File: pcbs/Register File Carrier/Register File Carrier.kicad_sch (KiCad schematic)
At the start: 2 parts, among them J1001 Conn_02x20_Odd_Even, J1002 Conn_02x20_Odd_Even

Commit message: Roughing a little more out
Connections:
- no-connect marks 22 -> 10
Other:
- sheet Connector Block ports: added A[0..15], B[0..15], CLK, C[0..15], R_{A}[0..3], R_{B}[0..3], R_{C}[0..3], ~{Active}; removed none
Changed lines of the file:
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@@
-	)
-	(no_connect
-		(at 26.67 128.27)
 	)
 	(no_connect
@@
 	)
 	(no_connect
-		(at 44.45 133.35)
-	)
-	(no_connect
 		(at 44.45 138.43)
-	)
-	(no_connect
-		(at 26.67 130.81)
-	)
-	(no_connect
-		(at 44.45 130.81)
-	)
-	(no_connect
-		(at 26.67 123.19)
-	)
-	(no_connect
-		(at 44.45 135.89)
 	)
 	(no_connect
@@
 	)
 	(no_connect
-		(at 26.67 125.73)
-	)
-	(no_connect
 		(at 29.21 76.2)
 	)
@@
 	)
 	(no_connect
-		(at 44.45 123.19)
-	)
-	(no_connect
 		(at 41.91 76.2)
-	)
-	(no_connect
-		(at 44.45 128.27)
 	)
 	(no_connect
@@
 	)
 	(no_connect
-		(at 26.67 133.35)
-	)
-	(no_connect
-		(at 26.67 135.89)
-	)
-	(no_connect
-		(at 44.45 125.73)
-	)
-	(no_connect
 		(at 41.91 143.51)
 	)
@@
 		)
 	)
+	(bus
+		(pts
+			(xy 127 115.57) (xy 137.16 115.57)
+		)
+		(stroke
+			(width 0)
+			(type default)
+		)
+	)
 	(wire
 		(pts
@@
 		)
 	)
+	(bus
+		(pts
+			(xy 127 118.11) (xy 137.16 118.11)
+		)
+		(stroke
+			(width 0)
+			(type default)
+		)
+	)
 	(wire
 		(pts
@@
 		(pts
 			(xy 26.67 138.43) (xy 29.21 138.43)
+		)
+		(stroke
+			(width 0)
+			(type default)
+		)
+	)
+	(bus
+		(pts
+			(xy 127 120.65) (xy 137.16 120.65)
 		)
 		(stroke
@@
 	)
 	(sheet
-		(at 137.16 92.71)
-		(size 107.95 73.66)
+		(at 137.16 114.3)
+		(size 36.83 54.61)
 		(fields_autoplaced yes)
 		(stroke
@@
 		)
 		(property "Sheetname" "Connector Block"
-			(at 137.16 91.9984 0)
+			(at 137.16 113.5884 0)
 			(effects
 				(font
@@
 		)
 		(property "Sheetfile" "connectors.kicad_sch"
-			(at 137.16 166.9546 0)
+			(at 137.16 169.4946 0)
 			(effects
 				(font
@@
 			)
 		)
+		(pin "~{Active}" input
+			(at 137.16 151.13 180)
+			(effects
+				(font
+					(size 1.27 1.27)
+				)
+				(justify left)
+			)
+		)
+		(pin "CLK" input
+			(at 137.16 148.59 180)
+			(effects
+				(font
+					(size 1.27 1.27)
+				)
+				(justify left)
+			)
+		)
+		(pin "C[0..15]" input
+			(at 137.16 146.05 180)
+			(effects
+				(font
+					(size 1.27 1.27)
+				)
+				(justify left)
+			)
+		)
+		(pin "R_{A}[0..3]" input
+			(at 137.16 115.57 180)
+			(effects
+				(font
+					(size 1.27 1.27)
+				)
+				(justify left)
+			)
+		)
+		(pin "R_{C}[0..3]" input
+			(at 137.16 120.65 180)
+			(effects
+				(font
+					(size 1.27 1.27)
+				)
+				(justify left)
+			)
+		)
+		(pin "R_{B}[0..3]" input
+			(at 137.16 118.11 180)
+			(effects
+				(font
+					(size 1.27 1.27)
+				)
+				(justify left)
+			)
+		)
+		(pin "A[0..15]" output
+			(at 137.16 128.27 180)
+			(effects
+				(font
+					(size 1.27 1.27)
+				)
+				(justify left)
+			)
+		)
+		(pin "B[0..15]" output
+			(at 137.16 132.08 180)
+			(effects
+				(font
+					(size 1.27 1.27)
+				)
+				(justify left)
+			)
+		)

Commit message: Working on register selectors
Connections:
- net I10 renamed R_{B}2
- net I11 renamed R_{B}3
- net I12 renamed R_{C}0
- net I13 renamed R_{C}1
- net I14 renamed R_{C}2
- net I15 renamed R_{C}3
- net I4 renamed R_{A}0
- net I5 renamed R_{A}1
- net I6 renamed R_{A}2
- net I7 renamed R_{A}3
- net I8 renamed R_{B}0
- net I9 renamed R_{B}1
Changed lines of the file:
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@@
-		)
-	)
-	(label "I7"
-		(at 44.45 125.73 0)
-		(fields_autoplaced yes)
-		(effects
-			(font
-				(size 1.27 1.27)
-			)
-			(justify left bottom)
 		)
 	)
@@
 		)
 	)
+	(label "R_{B}3"
+		(at 44.45 130.81 0)
+		(fields_autoplaced yes)
+		(effects
+			(font
+				(size 1.27 1.27)
+			)
+			(justify left bottom)
+		)
+	)
 	(label "C7"
 		(at 44.45 105.41 0)
@@
 		)
 	)
+	(label "R_{C}0"
+		(at 26.67 133.35 180)
+		(fields_autoplaced yes)
+		(effects
+			(font
+				(size 1.27 1.27)
+			)
+			(justify right bottom)
+		)
+	)
 	(label "A10"
 		(at 26.67 48.26 180)
@@
 		)
 	)
+	(label "R_{C}2"
+		(at 26.67 135.89 180)
+		(fields_autoplaced yes)
+		(effects
+			(font
+				(size 1.27 1.27)
+			)
+			(justify right bottom)
+		)
+	)
 	(label "Cycle1"
 		(at 44.45 138.43 0)
@@
 		)
 	)
-	(label "I9"
-		(at 44.45 128.27 0)
-		(fields_autoplaced yes)
-		(effects
-			(font
-				(size 1.27 1.27)
-			)
-			(justify left bottom)
-		)
-	)
-	(label "I6"
-		(at 26.67 125.73 180)
-		(fields_autoplaced yes)
-		(effects
-			(font
-				(size 1.27 1.27)
-			)
-			(justify right bottom)
+	(label "R_{B}2"
+		(at 26.67 130.81 180)
+		(fields_autoplaced yes)
+		(effects
+			(font
+				(size 1.27 1.27)
+			)
+			(justify right bottom)
+		)
+	)
+	(label "R_{C}1"
+		(at 44.45 133.35 0)
+		(fields_autoplaced yes)
+		(effects
+			(font
+				(size 1.27 1.27)
+			)
+			(justify left bottom)
 		)
 	)
@@
 		)
 	)
+	(label "R_{B}1"
+		(at 44.45 128.27 0)
+		(fields_autoplaced yes)
+		(effects
+			(font
+				(size 1.27 1.27)
+			)
+			(justify left bottom)
+		)
+	)
 	(label "B2"
 		(at 26.67 58.42 180)
@@
 		)
 	)
-	(label "I11"
-		(at 44.45 130.81 0)
-		(fields_autoplaced yes)
-		(effects
-			(font
-				(size 1.27 1.27)
-			)
-			(justify left bottom)
-		)
-	)
-	(label "I4"
+	(label "R_{A}0"
 		(at 26.67 123.19 180)
 		(fields_autoplaced yes)
@@
 		)
 	)
+	(label "R_{A}1"
+		(at 44.45 123.19 0)
+		(fields_autoplaced yes)
+		(effects
+			(font
+				(size 1.27 1.27)
+			)
+			(justify left bottom)
+		)
+	)
 	(label "C2"
 		(at 26.67 100.33 180)
@@
 		)
 	)
+	(label "R_{A}2"
+		(at 26.67 125.73 180)
+		(fields_autoplaced yes)
+		(effects
+			(font
+				(size 1.27 1.27)
+			)
+			(justify right bottom)
+		)
+	)
 	(label "A3"
 		(at 44.45 38.1 0)
@@
 		)
 	)
+	(label "R_{C}3"
+		(at 44.45 135.89 0)
+		(fields_autoplaced yes)
+		(effects
+			(font
+				(size 1.27 1.27)
+			)
+			(justify left bottom)
+		)
+	)
 	(label "I1"
 		(at 44.45 118.11 0)
@@
 		)
 	)
-	(label "I8"
-		(at 26.67 128.27 180)
-		(fields_autoplaced yes)
-		(effects
-			(font
-				(size 1.27 1.27)
-			)
-			(justify right bottom)
-		)
-	)
 	(label "A2"
 		(at 26.67 38.1 180)
@@
 		)
 	)
+	(label "R_{A}3"
+		(at 44.45 125.73 0)
+		(fields_autoplaced yes)
+		(effects
+			(font
+				(size 1.27 1.27)
+			)
+			(justify left bottom)
+		)
+	)
 	(label "A8"
 		(at 26.67 45.72 180)
@@
 		)
 	)
-	(label "I15"
-		(at 44.45 135.89 0)
-		(fields_autoplaced yes)
-		(effects
-			(font
-				(size 1.27 1.27)
-			)
-			(justify left bottom)
-		)
-	)
 	(label "C11"
 		(at 44.45 110.49 0)
@@
 		)
 	)
-	(label "I12"
-		(at 26.67 133.35 180)
-		(fields_autoplaced yes)
-		(effects
-			(font
-				(size 1.27 1.27)
-			)
-			(justify right bottom)
-		)
-	)
 	(label "C15"
 		(at 44.45 115.57 0)
@@
 		)
 	)
-	(label "I5"
-		(at 44.45 123.19 0)
-		(fields_autoplaced yes)
-		(effects
-			(font
-				(size 1.27 1.27)
-			)
-			(justify left bottom)
-		)
-	)
 	(label "B9"
 		(at 44.45 66.04 0)
@@
 		)
 	)
-	(label "I14"
-		(at 26.67 135.89 180)
-		(fields_autoplaced yes)
-		(effects
-			(font
-				(size 1.27 1.27)
-			)
-			(justify right bottom)
-		)
-	)
 	(label "B8"
 		(at 26.67 66.04 180)
@@
 		)
 	)
+	(label "R_{B}0"
+		(at 26.67 128.27 180)
+		(fields_autoplaced yes)
+		(effects
+			(font
+				(size 1.27 1.27)
+			)
+			(justify right bottom)
+		)
+	)
 	(label "C4"
 		(at 26.67 102.87 180)
@@
 		)
 	)
-	(label "I10"
-		(at 26.67 130.81 180)
-		(fields_autoplaced yes)
-		(effects
-			(font
-				(size 1.27 1.27)
-			)
-			(justify right bottom)
-		)
-	)
 	(label "C13"
 		(at 44.45 113.03 0)
-		(fields_autoplaced yes)
-		(effects
-			(font
-				(size 1.27 1.27)
-			)
-			(justify left bottom)
-		)
-	)
-	(label "I13"
-		(at 44.45 133.35 0)
 		(fields_autoplaced yes)
 		(effects
@@
 	(sheet
 		(at 137.16 114.3)
-		(size 36.83 54.61)
+		(size 22.86 34.29)
 		(fields_autoplaced yes)
 		(stroke
@@
 		)
 		(property "Sheetfile" "connectors.kicad_sch"
-			(at 137.16 169.4946 0)
+			(at 137.16 149.1746 0)
 			(effects
 				(font
@@
 		)
 		(pin "~{Active}" input
-			(at 137.16 151.13 180)
+			(at 137.16 140.97 180)
 			(effects
 				(font
@@
 		)
 		(pin "CLK" input
-			(at 137.16 148.59 180)
+			(at 137.16 138.43 180)
 			(effects
 				(font
@@
 		)
 		(pin "C[0..15]" input
-			(at 137.16 146.05 180)
-			(effects
-				(font
+			(at 137.16 134.62 180)
+			(effects
+				(font

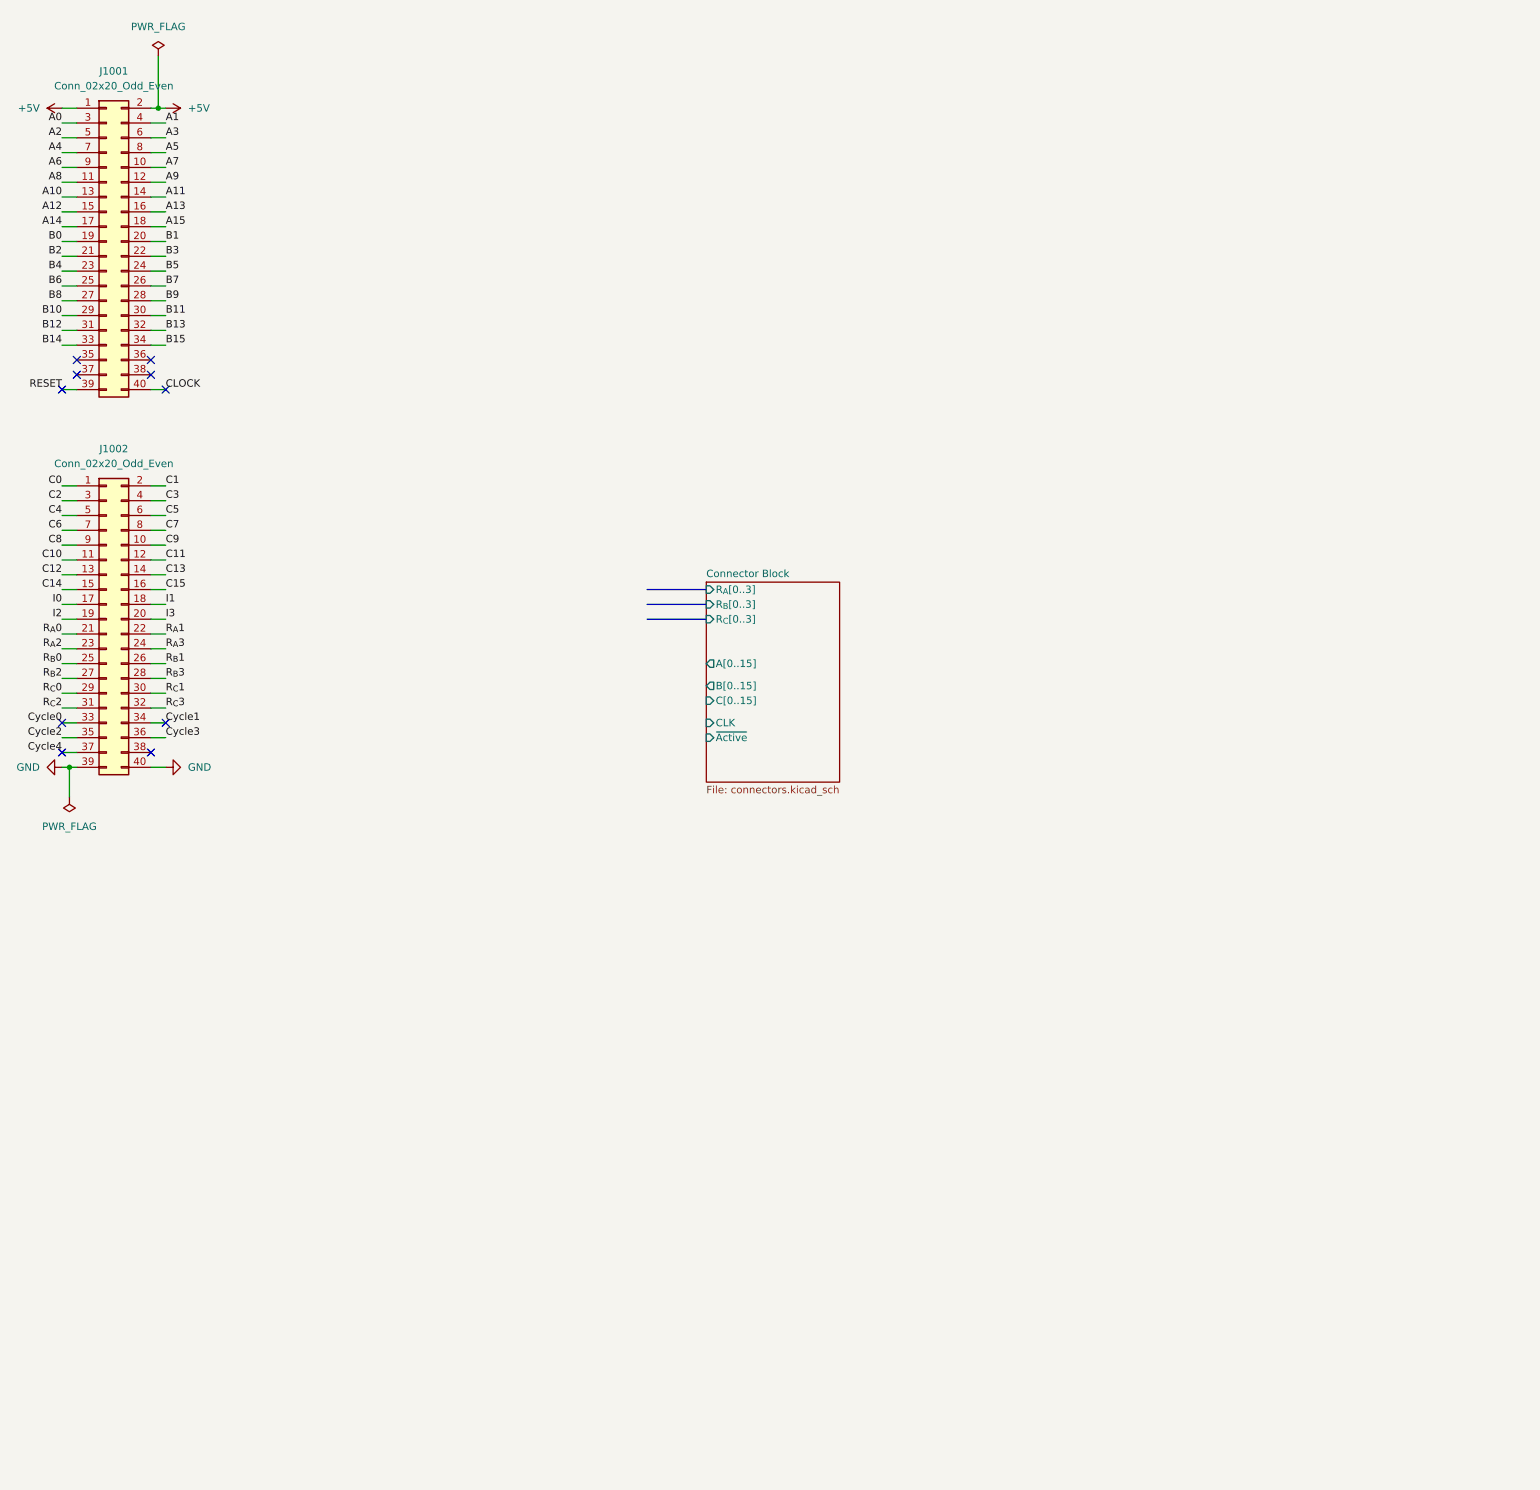
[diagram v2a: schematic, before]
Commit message: Thinking some things through
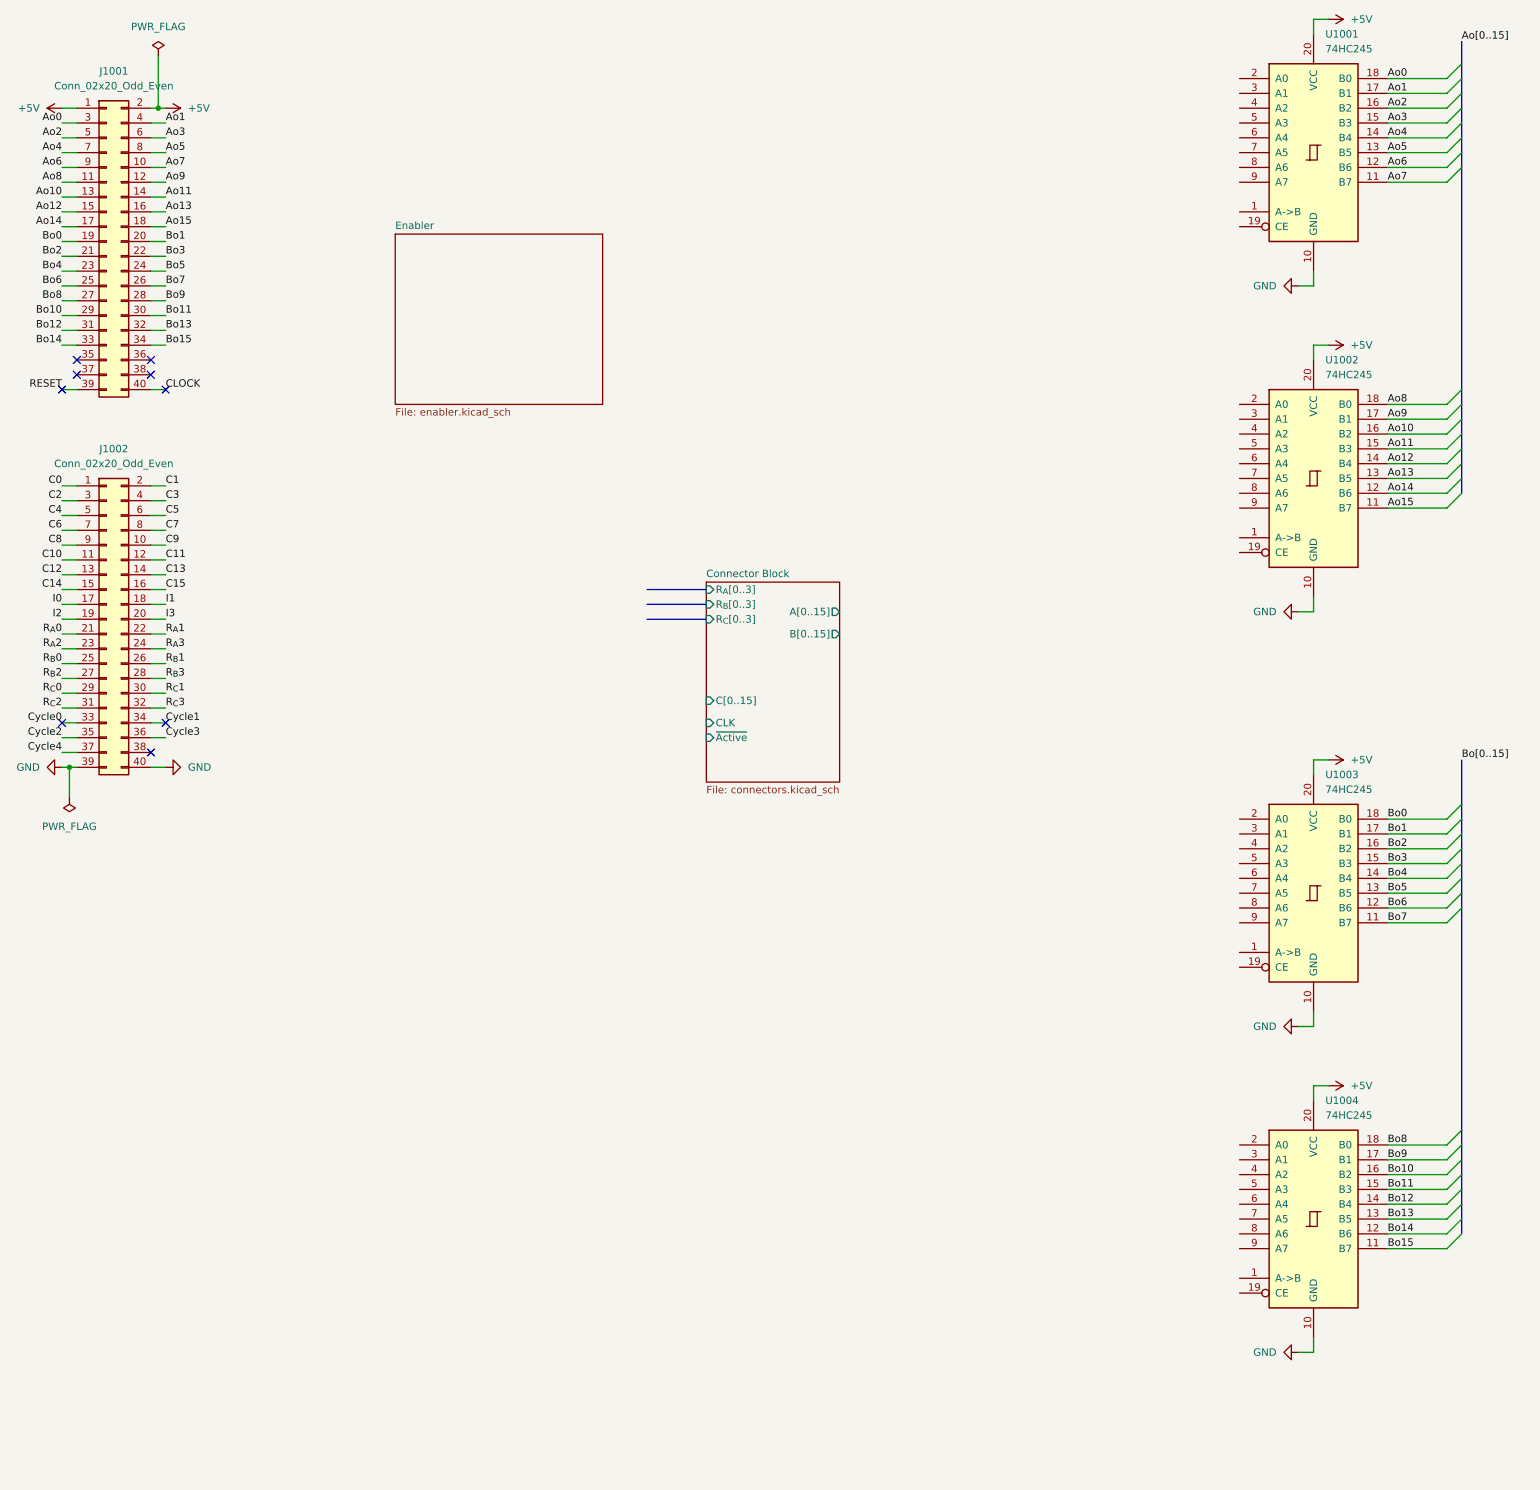
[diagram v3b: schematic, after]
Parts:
- added U1001, U1002, U1003, U1004: 74HC245, Package_SO:SOIC-20W_7.5x12.8mm_P1.27mm, symbol 74xx:74HC245
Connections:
- net +5V: now also U1001.20 (VCC), U1002.20 (VCC), U1003.20 (VCC), U1004.20 (VCC)
- net GND: now also U1001.10 (GND), U1002.10 (GND), U1003.10 (GND), U1004.10 (GND)
- net A0 renamed Ao0
- net Ao0: now also U1001.18 (B0)
- net A1 renamed Ao1
- net Ao1: now also U1001.17 (B1)
- net A10 renamed Ao10
- net Ao10: now also U1002.16 (B2)
- net A11 renamed Ao11
- net Ao11: now also U1002.15 (B3)
- net A12 renamed Ao12
- net Ao12: now also U1002.14 (B4)
- net A13 renamed Ao13
- net Ao13: now also U1002.13 (B5)
- net A14 renamed Ao14
- net Ao14: now also U1002.12 (B6)
- net A15 renamed Ao15
- net Ao15: now also U1002.11 (B7)
- net A2 renamed Ao2
- net Ao2: now also U1001.16 (B2)
- net A3 renamed Ao3
- net Ao3: now also U1001.15 (B3)
- net A4 renamed Ao4
- net Ao4: now also U1001.14 (B4)
- net A5 renamed Ao5
- net Ao5: now also U1001.13 (B5)
- net A6 renamed Ao6
- net Ao6: now also U1001.12 (B6)
- net A7 renamed Ao7
- net Ao7: now also U1001.11 (B7)
- net A8 renamed Ao8
- net Ao8: now also U1002.18 (B0)
- net A9 renamed Ao9
- net Ao9: now also U1002.17 (B1)
- net B0 renamed Bo0
- net Bo0: now also U1003.18 (B0)
- net B1 renamed Bo1
- net Bo1: now also U1003.17 (B1)
- net B10 renamed Bo10
- net Bo10: now also U1004.16 (B2)
- net B11 renamed Bo11
- net Bo11: now also U1004.15 (B3)
- net B12 renamed Bo12
- net Bo12: now also U1004.14 (B4)
- net B13 renamed Bo13
- net Bo13: now also U1004.13 (B5)
- net B14 renamed Bo14
- net Bo14: now also U1004.12 (B6)
- net B15 renamed Bo15
- net Bo15: now also U1004.11 (B7)
- net B2 renamed Bo2
- net Bo2: now also U1003.16 (B2)
- net B3 renamed Bo3
- net Bo3: now also U1003.15 (B3)
- net B4 renamed Bo4
- net Bo4: now also U1003.14 (B4)
- net B5 renamed Bo5
- net Bo5: now also U1003.13 (B5)
- net B6 renamed Bo6
- net Bo6: now also U1003.12 (B6)
- net B7 renamed Bo7
- net Bo7: now also U1003.11 (B7)
- net B8 renamed Bo8
- net Bo8: now also U1004.18 (B0)
- net B9 renamed Bo9
- net Bo9: now also U1004.17 (B1)
- no-connect marks 10 -> 9
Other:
- added sheet Enabler (enabler.kicad_sch)
